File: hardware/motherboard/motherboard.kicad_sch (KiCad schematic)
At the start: 31 parts, among them J3 RFShield_TwoPieces, U1 TART Correlator Socket, U15 74LVC1G04SE-7, U9 CS48520S, X2 1XXB16368MBA

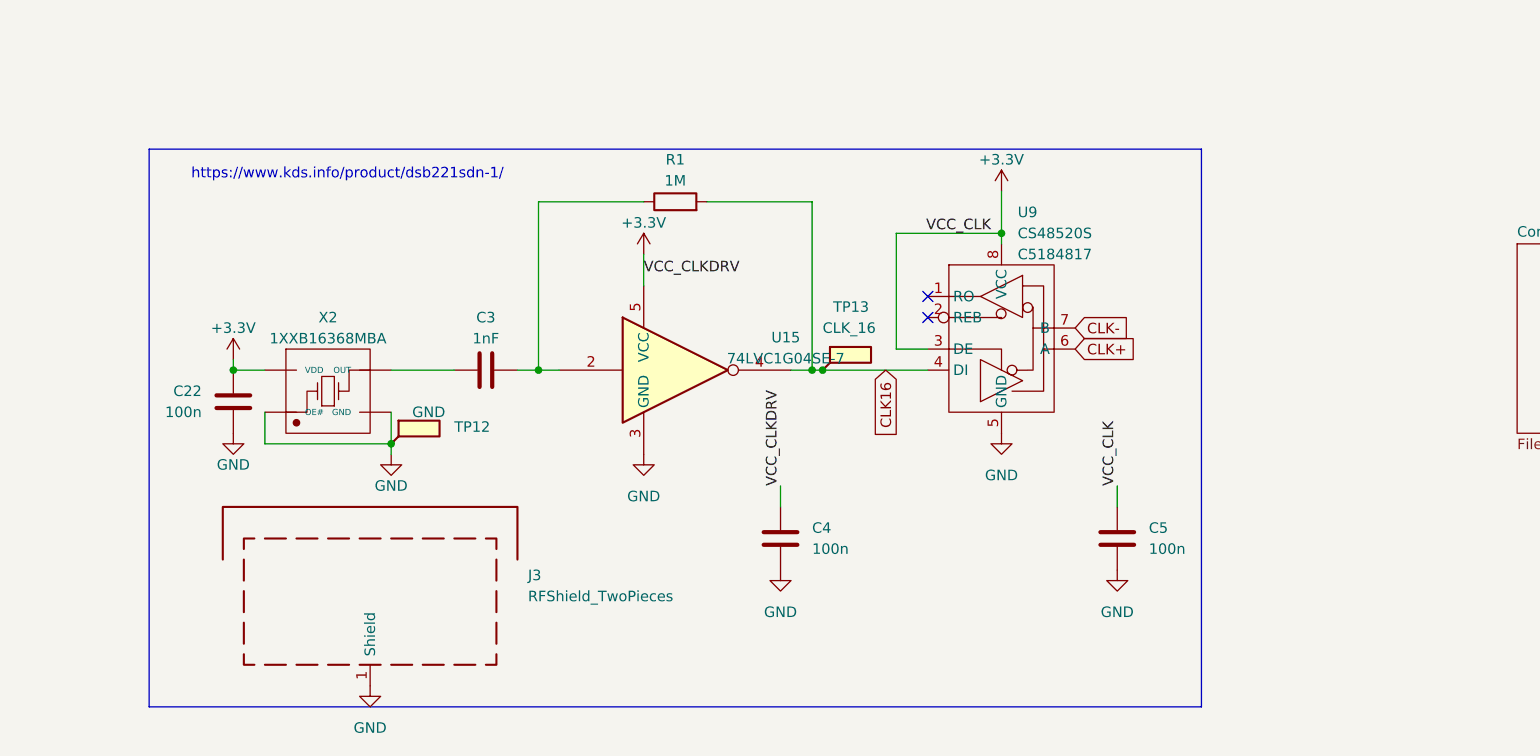
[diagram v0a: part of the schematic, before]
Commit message: add impedance matching resistors to RS485
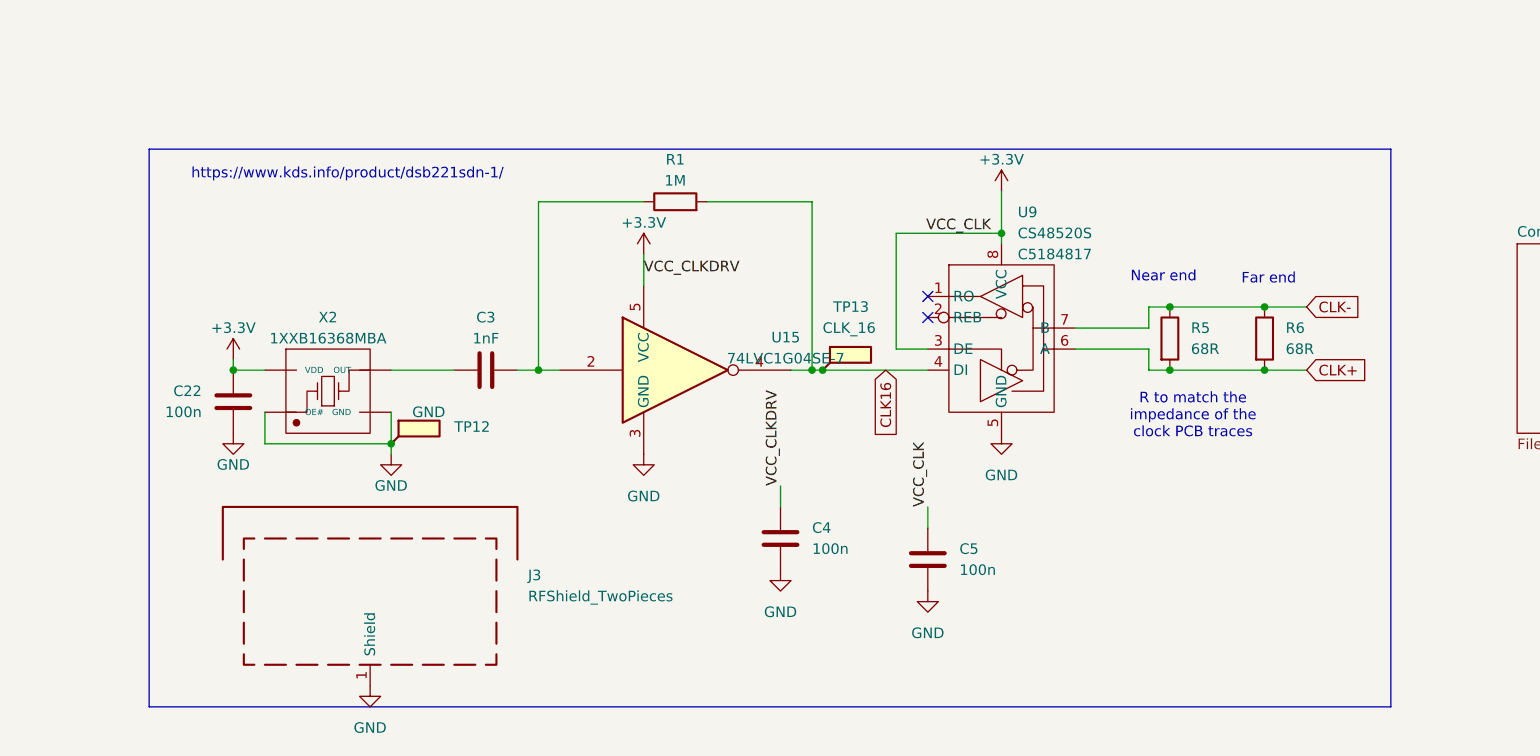
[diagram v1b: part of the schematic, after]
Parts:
- added R5, R6: 68R, Resistor_SMD:R_0402_1005Metric, symbol Device:R
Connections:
- net CLK+: now also R5.2, R6.2
- net CLK-: now also R5.1, R6.1
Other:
- note added: "Far end"
- note added: "Near end"
- note added: "R to match the impedance of the clock PCB traces"
- moved on the sheet: C5
